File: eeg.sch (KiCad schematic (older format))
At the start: 133 parts, among them J1 USB_B_Mini, U1 STM32F446RE, U10 -.+2.5V.+3.3V-GND, U11 +5V, U12 RN4678-V_RM100, U2 ADS1299-8CHANNEL, U3 RN42, U4 TPS73133DBV, U5 TPS73115DBV, U6 TPS60151DRV, U61 Electrode2, U7 DATA, U8 Electrode1, U9 ADC_REFGND_GPIO, Y1 16.00Mhz

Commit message: ERA-3A FOOTPRINT ADDED
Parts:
- R1, R10, R11, R12, R13, R14, R15, R16, R17, R18, R19, R2, R3, R4, R5, R6, R7, R8, R9: footprint Resistor_SMD:R_0603_1608Metric -> ERA-3A:RESC1608X55N
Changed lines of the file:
@@
 F 0 "R1" V 1605 11100 50  0000 C CNN
 F 1 "4.99k" V 1514 11100 50  0000 C CNN
-F 2 "Resistor_SMD:R_0603_1608Metric" H 1400 11100 50  0001 C CNN
+F 2 "ERA-3A:RESC1608X55N" H 1400 11100 50  0001 C CNN
 F 3 "~" H 1400 11100 50  0001 C CNN
 	1    1400 11100
@@
 F 0 "R6" V 1513 7850 50  0000 C CNN
 F 1 "4.99K" V 1300 7850 50  0000 C CNN
-F 2 "Resistor_SMD:R_0603_1608Metric" H 1400 7850 50  0001 C CNN
+F 2 "ERA-3A:RESC1608X55N" H 1400 7850 50  0001 C CNN
 F 3 "~" H 1400 7850 50  0001 C CNN
 	1    1400 7850
@@
 F 0 "R7" V 1605 8350 50  0000 C CNN
 F 1 "4.99k" V 1300 8350 50  0000 C CNN
-F 2 "Resistor_SMD:R_0603_1608Metric" H 1400 8350 50  0001 C CNN
+F 2 "ERA-3A:RESC1608X55N" H 1400 8350 50  0001 C CNN
 F 3 "~" H 1400 8350 50  0001 C CNN
 	1    1400 8350
@@
 F 0 "R2" V 1513 10100 50  0000 C CNN
 F 1 "4.99K" V 1300 10100 50  0000 C CNN
-F 2 "Resistor_SMD:R_0603_1608Metric" H 1400 10100 50  0001 C CNN
+F 2 "ERA-3A:RESC1608X55N" H 1400 10100 50  0001 C CNN
 F 3 "~" H 1400 10100 50  0001 C CNN
 	1    1400 10100
@@
 F 0 "R3" V 1500 10600 50  0000 C CNN
 F 1 "4.99k" V 1300 10600 50  0000 C CNN
-F 2 "Resistor_SMD:R_0603_1608Metric" H 1400 10600 50  0001 C CNN
+F 2 "ERA-3A:RESC1608X55N" H 1400 10600 50  0001 C CNN
 F 3 "~" H 1400 10600 50  0001 C CNN
 	1    1400 10600
@@
 F 0 "R18" V 3150 6800 50  0000 C CNN
 F 1 "4.99K" V 2950 6800 50  0000 C CNN
-F 2 "Resistor_SMD:R_0603_1608Metric" H 3050 6800 50  0001 C CNN
+F 2 "ERA-3A:RESC1608X55N" H 3050 6800 50  0001 C CNN
 F 3 "~" H 3050 6800 50  0001 C CNN
 	1    3050 6800
@@
 F 0 "R19" V 3150 7300 50  0000 C CNN
 F 1 "4.99k" V 2950 7300 50  0000 C CNN
-F 2 "Resistor_SMD:R_0603_1608Metric" H 3050 7300 50  0001 C CNN
+F 2 "ERA-3A:RESC1608X55N" H 3050 7300 50  0001 C CNN
 F 3 "~" H 3050 7300 50  0001 C CNN
 	1    3050 7300
@@
 F 0 "R16" V 3150 7850 50  0000 C CNN
 F 1 "4.99K" V 2950 7850 50  0000 C CNN
-F 2 "Resistor_SMD:R_0603_1608Metric" H 3050 7850 50  0001 C CNN
+F 2 "ERA-3A:RESC1608X55N" H 3050 7850 50  0001 C CNN
 F 3 "~" H 3050 7850 50  0001 C CNN
 	1    3050 7850
@@
 F 0 "R17" V 3150 8350 50  0000 C CNN
 F 1 "4.99k" V 2950 8350 50  0000 C CNN
-F 2 "Resistor_SMD:R_0603_1608Metric" H 3050 8350 50  0001 C CNN
+F 2 "ERA-3A:RESC1608X55N" H 3050 8350 50  0001 C CNN
 F 3 "~" H 3050 8350 50  0001 C CNN
 	1    3050 8350
@@
 F 0 "R5" V 1500 9500 50  0000 C CNN
 F 1 "4.99k" V 1300 9500 50  0000 C CNN
-F 2 "Resistor_SMD:R_0603_1608Metric" H 1400 9500 50  0001 C CNN
+F 2 "ERA-3A:RESC1608X55N" H 1400 9500 50  0001 C CNN
 F 3 "~" H 1400 9500 50  0001 C CNN
 	1    1400 9500
@@
 F 0 "R4" V 1500 9000 50  0000 C CNN
 F 1 "4.99K" V 1300 9000 50  0000 C CNN
-F 2 "Resistor_SMD:R_0603_1608Metric" H 1400 9000 50  0001 C CNN
+F 2 "ERA-3A:RESC1608X55N" H 1400 9000 50  0001 C CNN
 F 3 "~" H 1400 9000 50  0001 C CNN
 	1    1400 9000
@@
 F 0 "R15" V 3150 9500 50  0000 C CNN
 F 1 "4.99k" V 2950 9500 50  0000 C CNN
-F 2 "Resistor_SMD:R_0603_1608Metric" H 3050 9500 50  0001 C CNN
+F 2 "ERA-3A:RESC1608X55N" H 3050 9500 50  0001 C CNN
 F 3 "~" H 3050 9500 50  0001 C CNN
 	1    3050 9500
@@
 F 0 "R14" V 3163 9000 50  0000 C CNN
 F 1 "4.99K" V 2950 9000 50  0000 C CNN
-F 2 "Resistor_SMD:R_0603_1608Metric" H 3050 9000 50  0001 C CNN
+F 2 "ERA-3A:RESC1608X55N" H 3050 9000 50  0001 C CNN
 F 3 "~" H 3050 9000 50  0001 C CNN
 	1    3050 9000
@@
 F 0 "R13" V 3255 10600 50  0000 C CNN
 F 1 "4.99k" V 2950 10600 50  0000 C CNN
-F 2 "Resistor_SMD:R_0603_1608Metric" H 3050 10600 50  0001 C CNN
+F 2 "ERA-3A:RESC1608X55N" H 3050 10600 50  0001 C CNN
 F 3 "~" H 3050 10600 50  0001 C CNN
 	1    3050 10600
@@
 F 0 "R12" V 3163 10100 50  0000 C CNN
 F 1 "4.99K" V 2950 10100 50  0000 C CNN
-F 2 "Resistor_SMD:R_0603_1608Metric" H 3050 10100 50  0001 C CNN
+F 2 "ERA-3A:RESC1608X55N" H 3050 10100 50  0001 C CNN
 F 3 "~" H 3050 10100 50  0001 C CNN
 	1    3050 10100
@@
 F 0 "R8" V 1513 6800 50  0000 C CNN
 F 1 "4.99K" V 1300 6800 50  0000 C CNN
-F 2 "Resistor_SMD:R_0603_1608Metric" H 1400 6800 50  0001 C CNN
+F 2 "ERA-3A:RESC1608X55N" H 1400 6800 50  0001 C CNN
 F 3 "~" H 1400 6800 50  0001 C CNN
 	1    1400 6800
@@
 F 0 "R9" V 1605 7300 50  0000 C CNN
 F 1 "4.99k" V 1300 7300 50  0000 C CNN
-F 2 "Resistor_SMD:R_0603_1608Metric" H 1400 7300 50  0001 C CNN
+F 2 "ERA-3A:RESC1608X55N" H 1400 7300 50  0001 C CNN
 F 3 "~" H 1400 7300 50  0001 C CNN
 	1    1400 7300
@@
 F 0 "R11" V 3255 11600 50  0000 C CNN
 F 1 "4.99k" V 2950 11600 50  0000 C CNN
-F 2 "Resistor_SMD:R_0603_1608Metric" H 3050 11600 50  0001 C CNN
+F 2 "ERA-3A:RESC1608X55N" H 3050 11600 50  0001 C CNN
 F 3 "~" H 3050 11600 50  0001 C CNN
 	1    3050 11600
@@
 F 0 "R10" V 3150 11100 50  0000 C CNN
 F 1 "4.99K" V 2950 11100 50  0000 C CNN
-F 2 "Resistor_SMD:R_0603_1608Metric" H 3050 11100 50  0001 C CNN
+F 2 "ERA-3A:RESC1608X55N" H 3050 11100 50  0001 C CNN
 F 3 "~" H 3050 11100 50  0001 C CNN
 	1    3050 11100

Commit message: Voltage Regulator Connection Fixed
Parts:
- removed C22, C25, C27, C28, C31, C32, C35, C37, C55: 1uF, Capacitor_SMD:C_0603_1608Metric, symbol Device:C_Small
- removed C23, C24, C26, C29, C30, C33, C36, C39: 10uF, Capacitor_SMD:C_0603_1608Metric, symbol Device:C_Small
- removed C34, C38: 2.2uF, Capacitor_SMD:C_0603_1608Metric, symbol Device:C_Small
- removed C43, C44: 0.1uF, Capacitor_Tantalum_SMD:CP_EIA-1608-08_AVX-J_Pad1.25x1.05mm_HandSolder, symbol Device:C_Small
- removed D5: LED, LED_SMD:LED_0603_1608Metric_Pad1.05x0.95mm_HandSolder, symbol Device:LED
- removed R23: 210K, Resistor_SMD:R_0603_1608Metric, symbol Device:R_Small_US
- removed R24: 100K, Resistor_SMD:R_0603_1608Metric, symbol Device:R_Small_US
- removed R25: 10K, Resistor_SMD:R_0603_1608Metric, symbol Device:R_Small_US
- removed U3: RN42, RF_Module:RN42, symbol RF_Bluetooth:RN42
- removed U4: TPS73133DBV, Package_TO_SOT_SMD:SOT-23-5, symbol Regulator_Linear:TPS73133DBV
- removed U5: TPS73115DBV, Package_TO_SOT_SMD:SOT-23-5, symbol Regulator_Linear:TPS73115DBV
- removed U6: TPS60151DRV, Package_SON:WSON-6-1EP_2x2mm_P0.65mm_EP1x1.6mm_ThermalVias, symbol Regulator_SwitchedCapacitor:TPS60151DRV
- added C100, C102: 1uF_X5R_0603, symbol Device:C_Small
- added C101, C103: 100nF, symbol Device:C_Small
- added C104, C105, C109, C110, C114, C115, C119, C120: 10uF, symbol Device:C_Small
- added C106, C107, C108, C112: 1uF, symbol Device:C_Small
- added C111: C_Small, symbol Device:C_Small
- added C113, C116, C118: 2.2uF, symbol Device:C_Small
- added C117: 0.01uF, symbol Device:C_Small
- added L1, L2, L4, L5: 3.3uH, INDC2012X87N, symbol MLZ2012A3R3WT000:MLZ2012A3R3WT000
- added U?: LD39050PU33R, SON95P300X300X100-7N, symbol LD39050PU33R:LD39050PU33R
- added U?: TPS60403DBVT, SOT95P280X145-5N, symbol TPS60403DBVT:TPS60403DBVT
- added U?: TPS73225DBVT, SOT95P280X145-5N, symbol TPS73225DBVT:TPS73225DBVT
- added U?: TPS72325DBVT, SOT95P280X145-5N, symbol TPS72325DBVT:TPS72325DBVT
- HC736: footprint Oscillator:Oscillator_SMD_Abracon_ASE-4Pin_3.2x2.5mm -> ERA-3A:OSCCC500X320X150N
- Y1: footprint Crystal:Crystal_HC49-4H_Vertical -> Crystal:Crystal_SMD_5032-4Pin_5.0x3.2mm
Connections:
- net labels added: -5V, RN46CTS
- net labels removed: -5v_UNREG, RN42CTS, RN42RTS, RN42STATUS, USART1RX, USART1TX
- wire segments 486 -> 487
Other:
- moved on the sheet: C1001, C20, D6, D7, R30, R31, U10, U11, U12, U7, U9

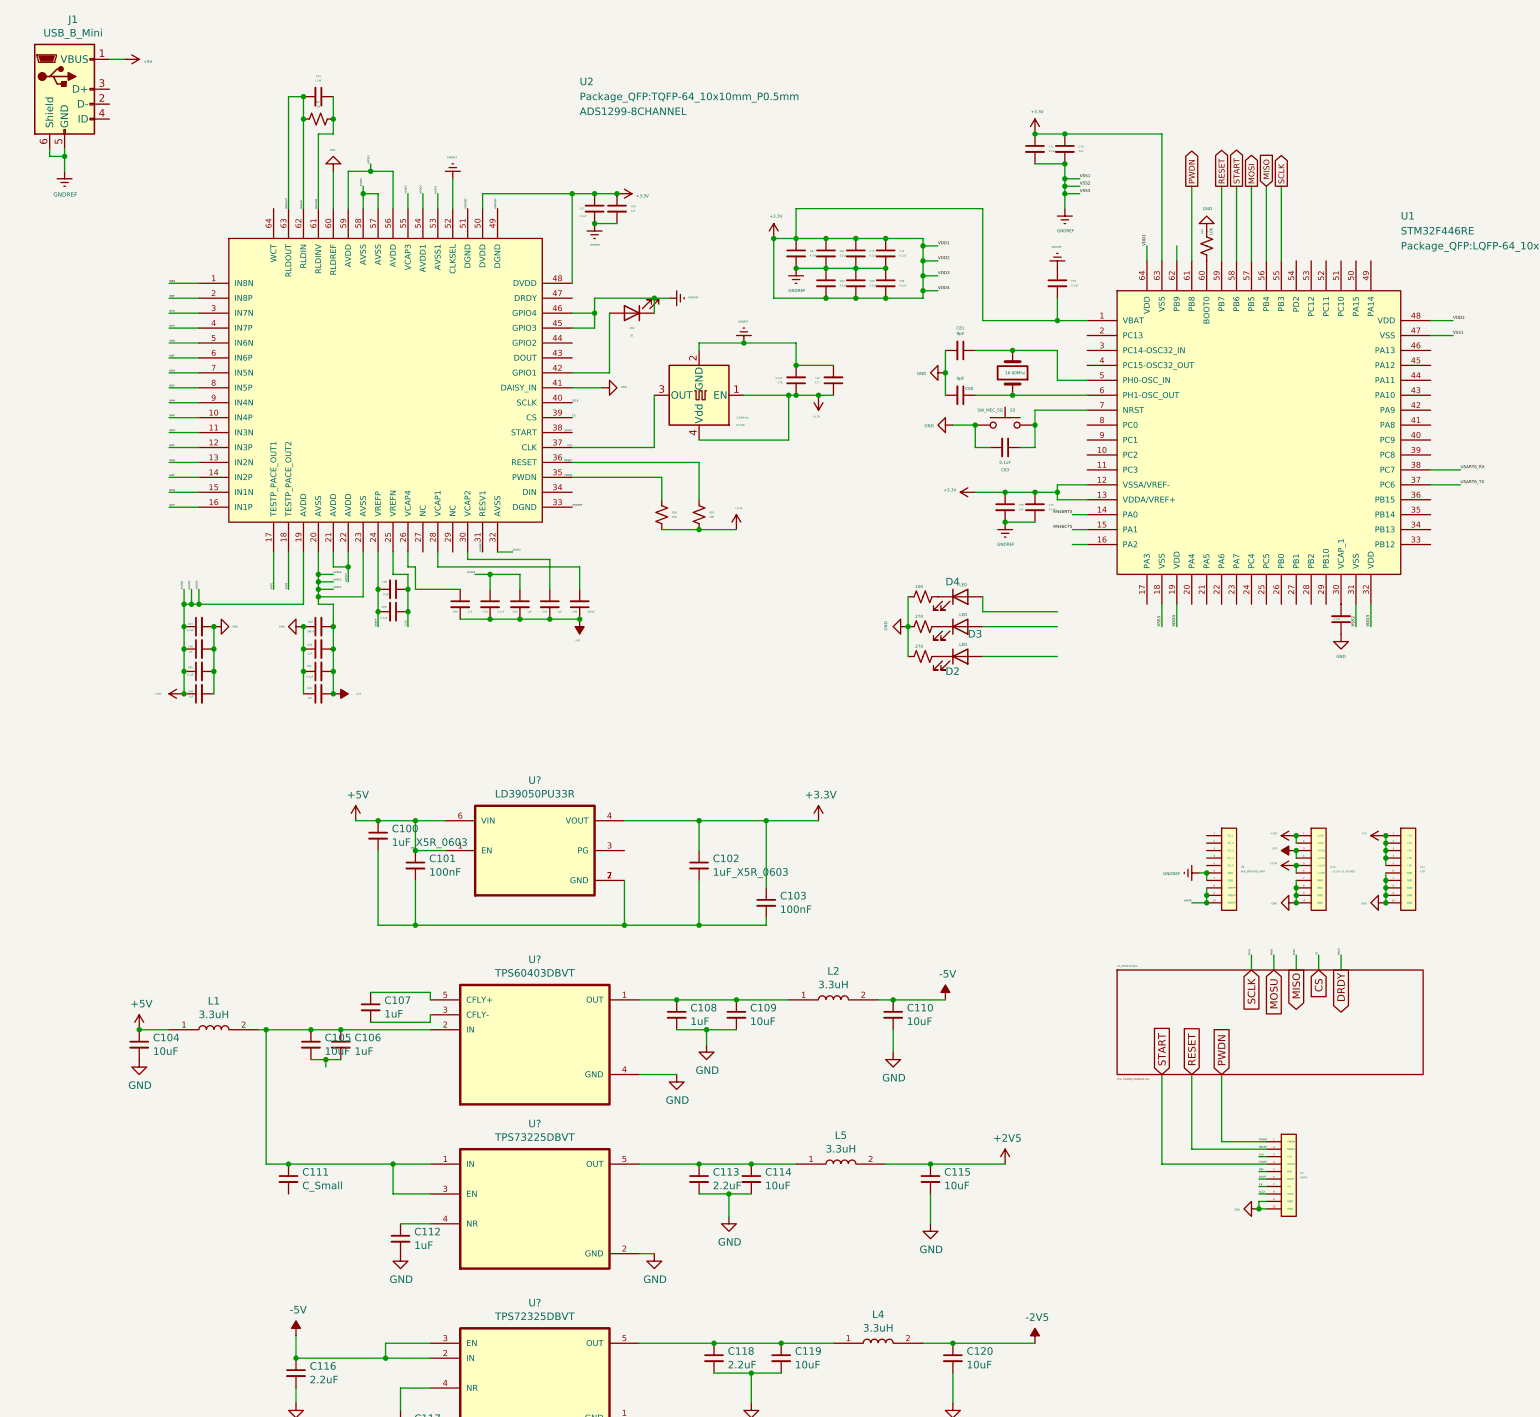
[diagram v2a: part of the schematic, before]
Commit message: Added capacitor footprints redrawed voltage regulators
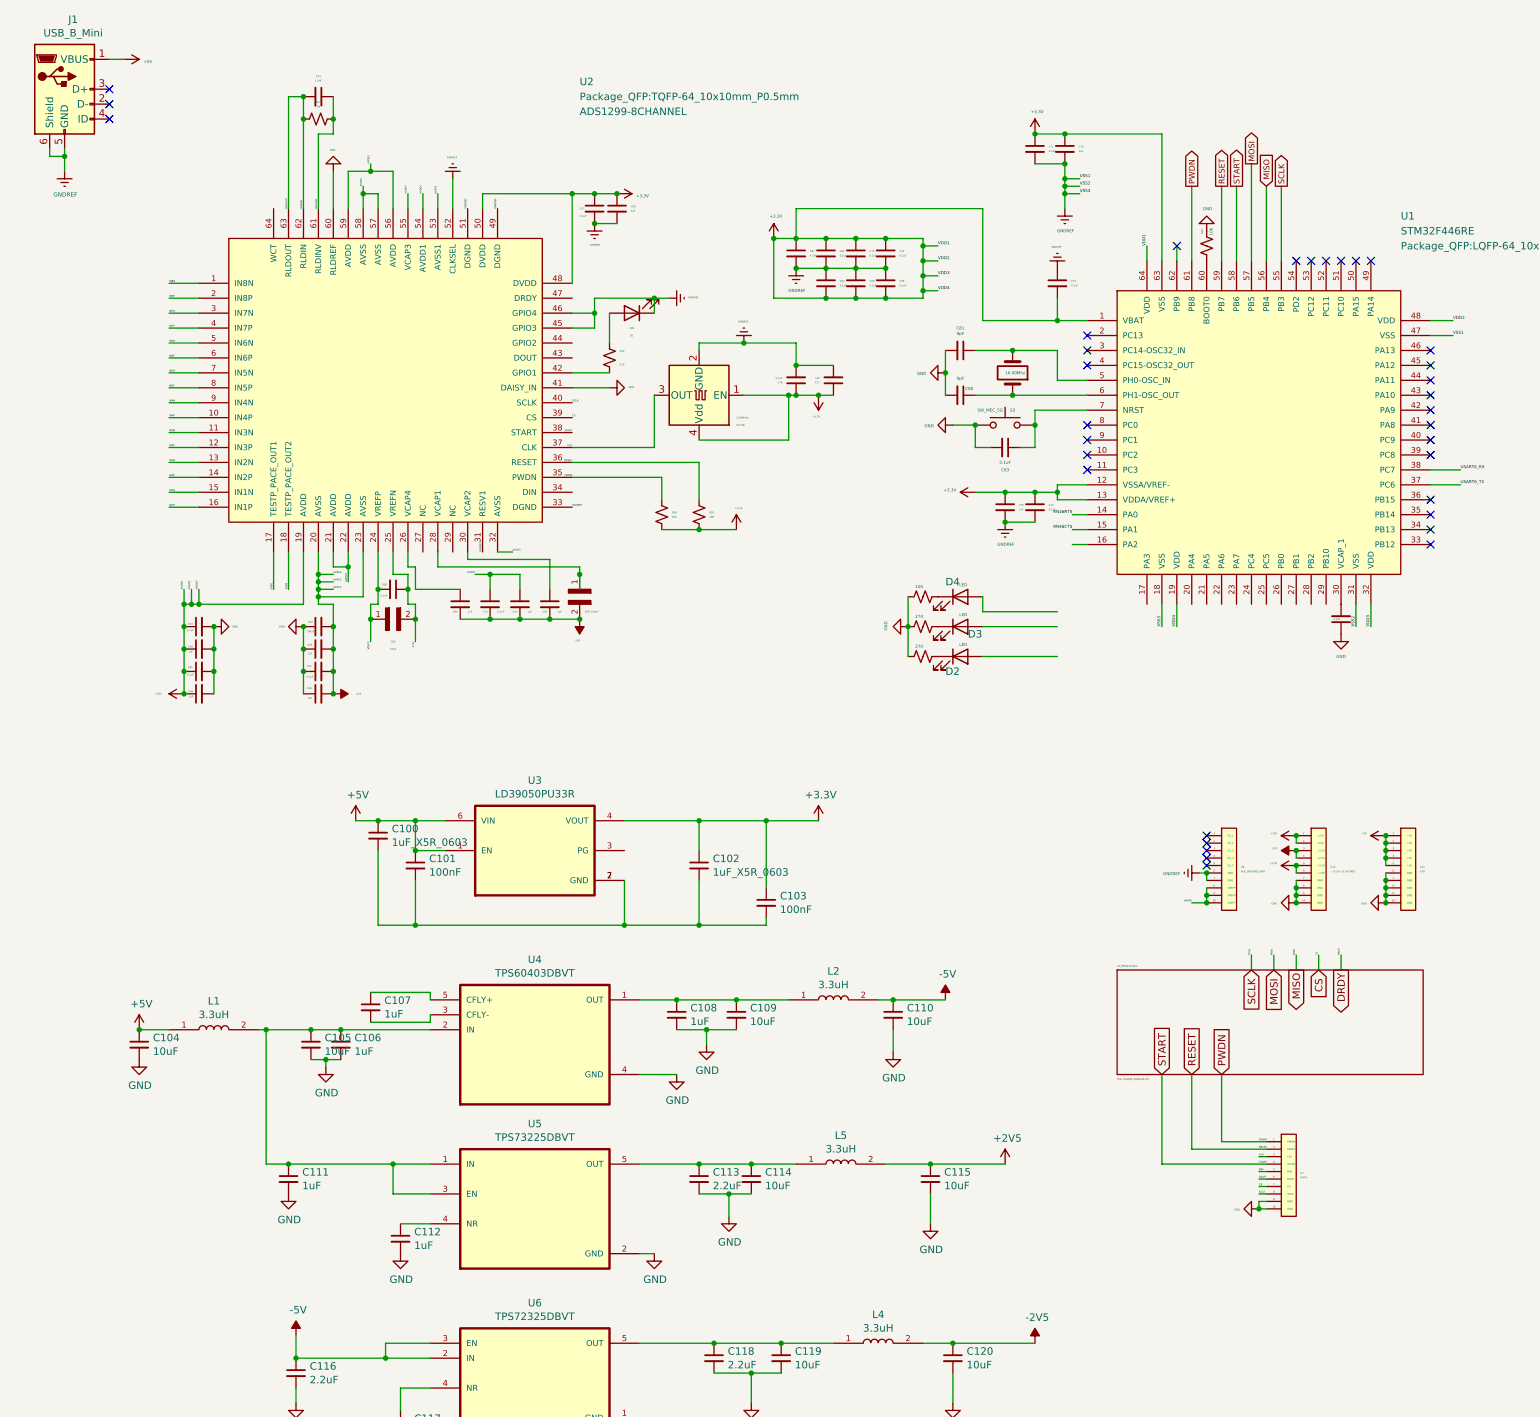
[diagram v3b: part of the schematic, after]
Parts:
- removed C65: 10uF, Capacitor_SMD:C_0603_1608Metric, symbol Device:C_Small
- removed C69: 100uF, Capacitor_SMD:C_0603_1608Metric, symbol Device:C_Small
- added C65: 10uF, TCA1C106M8R:RESC3216X65N, symbol TCA1C106M8R:TCA1C106M8R
- added C69: 100uF, TCA1C106M8R:RESC3216X65N, symbol TCA1C106M8R:TCA1C106M8R
- added R32: 270, Resistor_SMD:R_0603_1608Metric, symbol Device:R_Small_US
- C100, C102: footprint (none) -> 06033D105KAT2A:CAPC1608X94N
- C101, C103: footprint (none) -> C0402C104K4RACTU:CAPC1005X55N
- C104, C105, C106, C107, C108, C109, C110, C112, C113, C114, C115, C116, C117, C118, C119, C120: footprint (none) -> Capacitor_SMD:C_0603_1608Metric
- C111: value C_Small -> 1uF; footprint (none) -> Capacitor_SMD:C_0603_1608Metric
- C67: footprint Capacitor_SMD:C_0603_1608Metric -> TCA1C106M8R:RESC3216X65N
- D7: footprint (none) -> LED_SMD:LED_0603_1608Metric
- L1, L2, L4, L5: footprint INDC2012X87N -> MLZ2012A3R3WT000:INDC2012X87N
- R27: footprint (none) -> ERA-6AEB105V:RESC2012X60N
- R28, R29: footprint (none) -> ERA-3A:RESC1608X55N
- U3: renamed from U?; footprint SON95P300X300X100-7N -> LD39050PU33R:SON95P300X300X100-7N
- gave numbers to parts that had none: 3
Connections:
- net -2.5V: now also C65.2
- net -2V5: now also C69.2
- net GND: now also C105.2, C106.2, C111.2
- net VREFP: now also C65.1
- net at U2.28 (VCAP1): now also C69.1
- net at U2.42 (GPIO1): now also R32.1; no longer D1.2 (A)
- new net: D1.2 (A), R32.2
- no-connect marks 0 -> 34
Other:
- moved on the sheet: C68

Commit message: ADS1299 Symbol and Footprint Changed, AVDD and ADSS PINS NEED TO FIX
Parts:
- added C21: 100uF, Capacitor_SMD:C_0603_1608Metric, symbol Device:C_Small
- added C22, C24, C26, C30, C31: 1uF, Capacitor_SMD:C_0603_1608Metric, symbol Device:C_Small
- added C23, C28, C29: 0.1uF, Capacitor_SMD:C_0603_1608Metric, symbol Device:C_Small
- added C25: 10uF, TCA1C106M8R:RESC3216X65N, symbol TCA1C106M8R:TCA1C106M8R
- added C27: 1.5nF, Capacitor_SMD:C_0805_2012Metric, symbol Device:C_Small
- added C32: 100uF, TCA1C106M8R:RESC3216X65N, symbol TCA1C106M8R:TCA1C106M8R
- added R23, R25: 10K, ERA-3A:RESC1608X55N, symbol Device:R_Small_US
- added R24: 1M, ERA-6AEB105V:RESC2012X60N, symbol Device:R_Small_US
- added U13: ADS1299IPAG, QFP50P1200X1200X120-64N, symbol ADS1299IPAG:ADS1299IPAG
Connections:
- net -2V5: now also C25.1, C26.1, C28.2, C29.2, C30.2, C31.1, C32.2, U13.25 (VREFN)
- net BIASIN: now also C27.1, R24.1, U13.62 (BIASIN), U13.63 (BIASOUT)
- net GND: now also U13.31 (RESV1), U13.33 (DGND), U13.41 (DAISY_IN), U13.49 (DGND), U13.51 (DGND), U13.60 (BIASREF)
- net IN1N: now also U13.15 (IN1N)
- net IN1P: now also U13.16 (IN1P)
- net IN2N: now also U13.13 (IN2N)
- net IN2P: now also U13.14 (IN2P)
- net IN3N: now also U13.11 (IN3N)
- net IN3P: now also U13.12 (IN3P)
- net IN4N: now also U13.9 (IN4N)
- net IN4P: now also U13.10 (IN4P)
- net IN5N: now also U13.7 (IN5N)
- net IN5P: now also U13.8 (IN5P)
- net IN6N: now also U13.5 (IN6N)
- net IN6P: now also U13.6 (IN6P)
- net IN7N: now also U13.3 (IN7N)
- net IN7P: now also U13.4 (IN7P)
- net IN8N: now also U13.1 (IN8N)
- net IN8P: now also U13.2 (IN8P)
- net SCLK: now also U13.40 (SCLK)
- net SRB1: now also U13.17 (SRB1)
- net SRB2: now also U13.18 (SRB2); no longer U2.18 (TESTP_PACE_OUT2)
- net START: now also U13.38 (START)
- net VREFP: now also C25.2, C28.1, U13.24 (VREFP)
- new net: U13.19 (AVDD@1), U13.21 (AVDD@1), U13.22 (AVDD@1), U13.56 (AVDD@1)
- new net: U13.20 (AVSS@1), U13.23 (AVSS@1), U13.32 (AVSS@1), U13.57 (AVSS@1)
- new net: C30.1, U13.26 (VCAP4)
- new net: C32.1, U13.28 (VCAP1)
- new net: C31.2, U13.30 (VCAP2)
- new net: R25.2, U13.35 (~PWDN)
- new net: R23.2, U13.36 (~RESET)
- new net: U13.48 (DVDD), U13.50 (DVDD)
- new net: C26.2, C29.1, U13.55 (VCAP3)
- new net: C27.2, R24.2, U13.61 (BIASINV)
- new net 3.3V: R23.1, R25.1
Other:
- moved on the sheet: C100, C101, C102, C103, C104, C105, C106, C107, C108, C109, C110, C111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
